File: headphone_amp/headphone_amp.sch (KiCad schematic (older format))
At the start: 41 parts, among them J1 Molex_SL_01x02_Male, J2 Molex_SL_01x02_Male, J3 Molex_SL_01x03_Male, J4 Molex_SL_01x03_Male, Q1 PZTA42, Q2 PZTA92, Q3 PZTA42, Q4 PZTA92, U1 NE5532

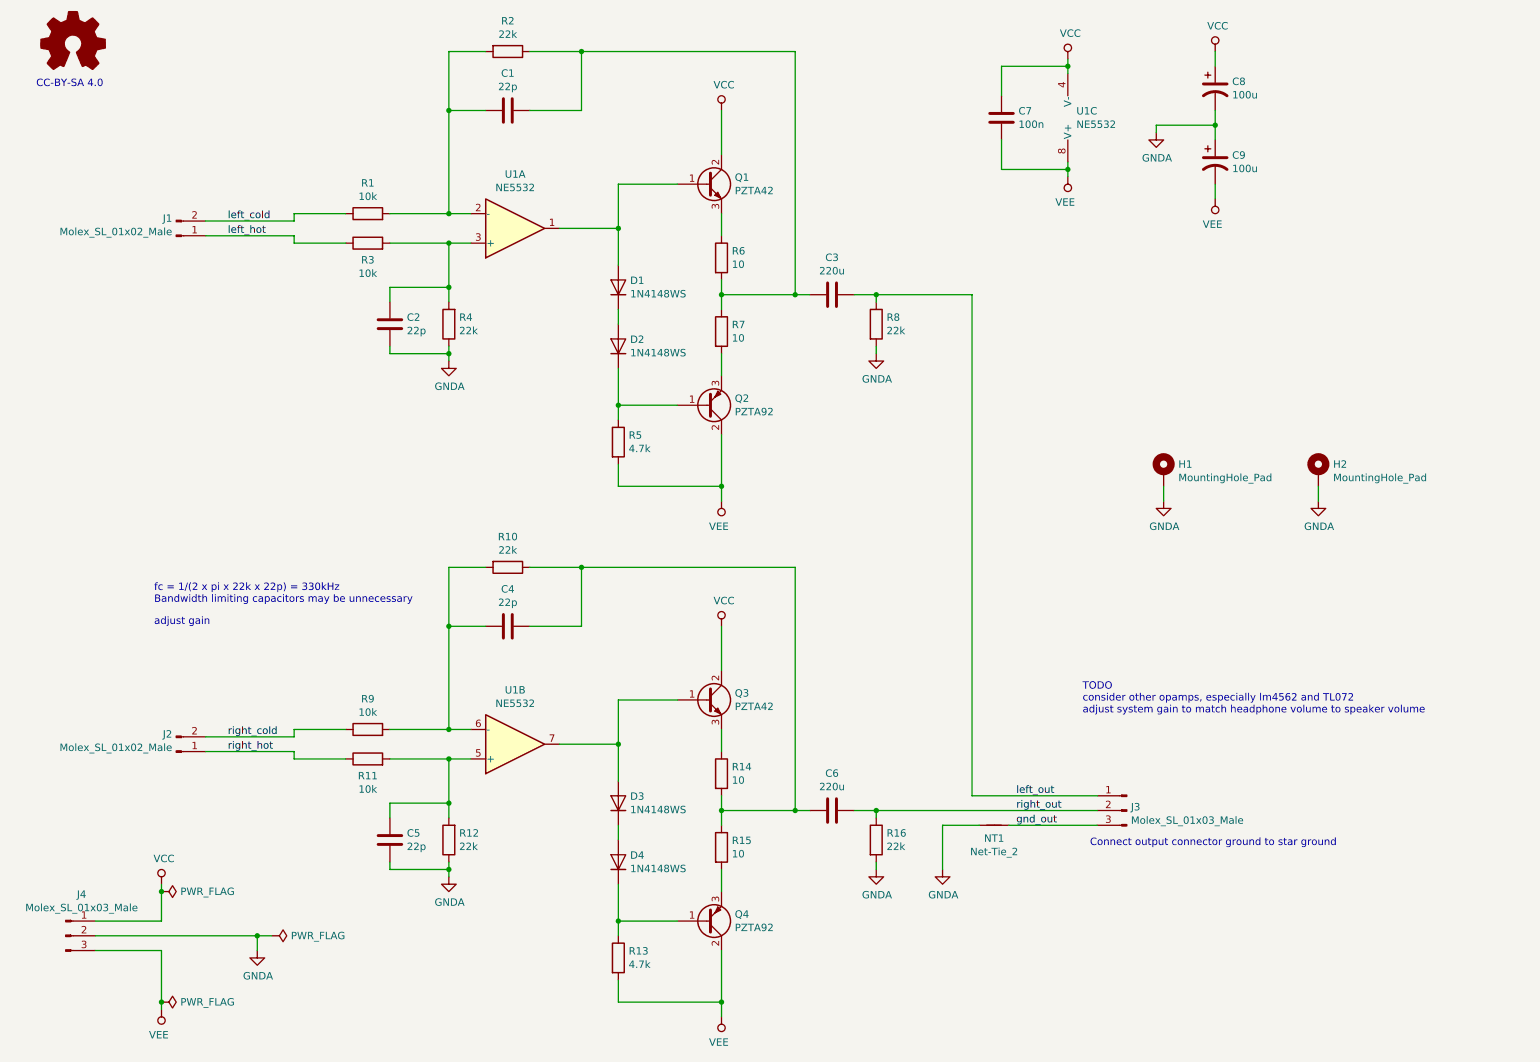
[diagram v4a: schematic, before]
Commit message: Update Headphone Amp to fix opamp power supplies
* fix opamp power supply connections. VCC was connected to V-, VEE to
V+. Fixed.
* re-layout opamp section to reflect above fix.
* right and left input connectors swapped to allow above fix.
* update schematic/layout date & revision in title block, and in board
silk.
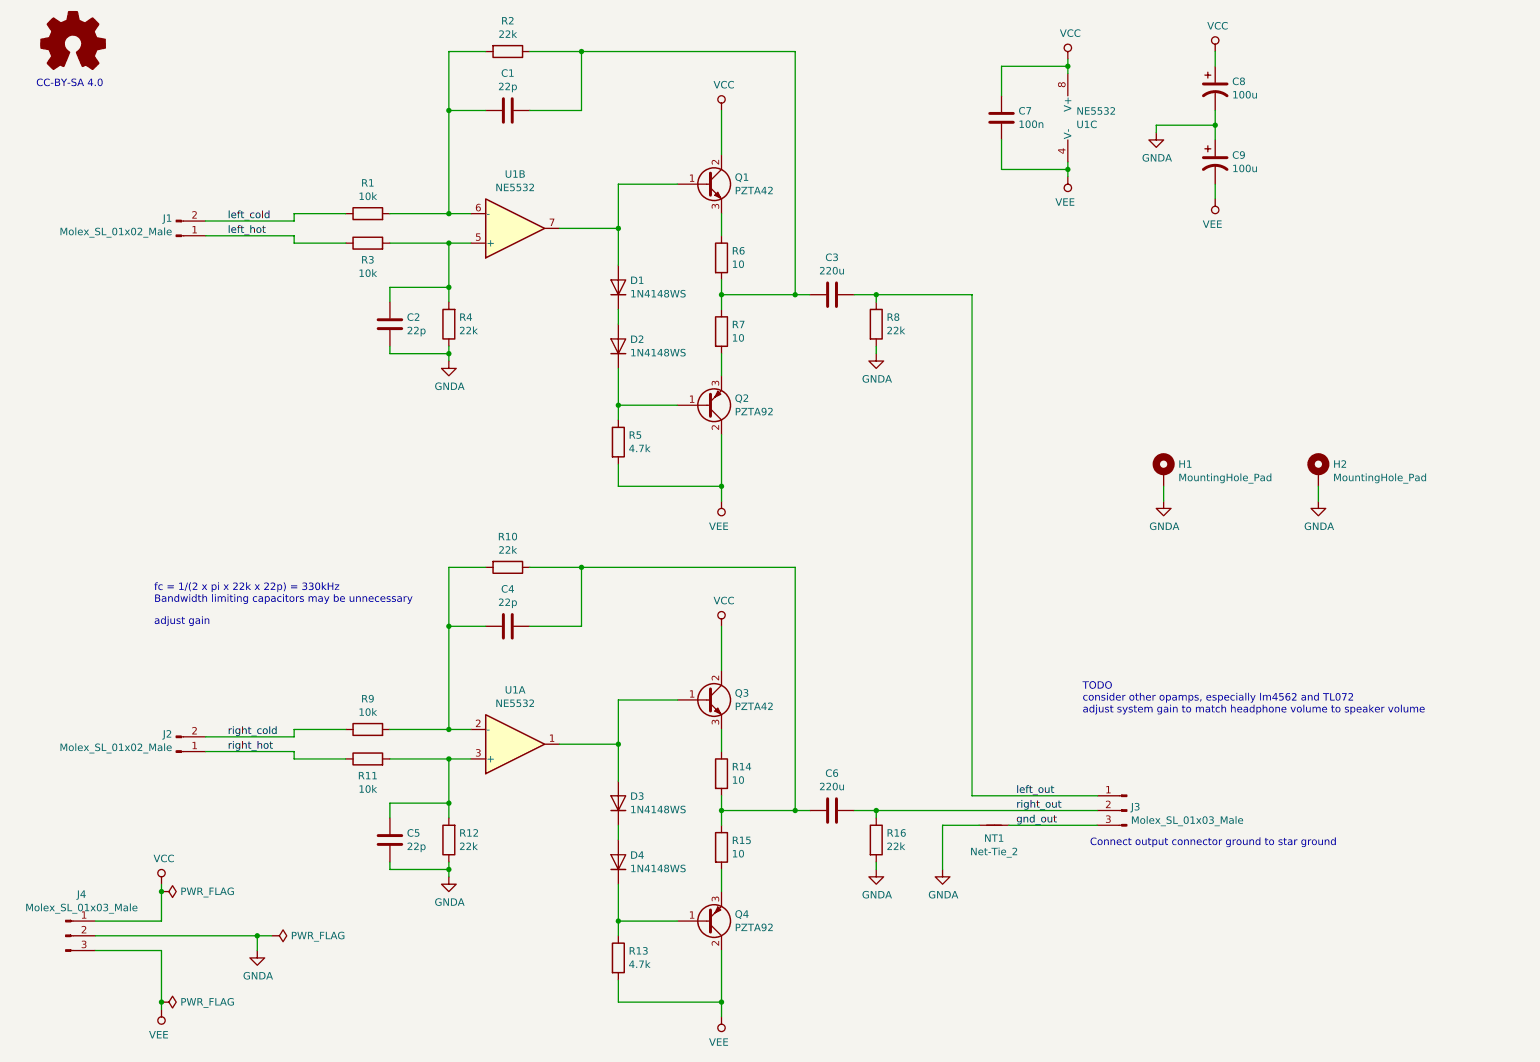
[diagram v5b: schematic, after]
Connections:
- net VCC: now also U1.8 (V+); no longer U1.4 (V-)
- net VEE: now also U1.4 (V-); no longer U1.8 (V+)
- net at D1.2 (A), Q1.1 (B): now also U1.7; no longer U1.1
- net at C1.2, R1.2, R2.2: now also U1.6 (-); no longer U1.2 (-)
- net at C2.1, R3.2, R4.2: now also U1.5 (+); no longer U1.3 (+)
- net at D3.2 (A), Q3.1 (B): now also U1.1; no longer U1.7
- net at C4.2, R10.2, R9.2: now also U1.2 (-); no longer U1.6 (-)
- net at C5.1, R11.2, R12.2: now also U1.3 (+); no longer U1.5 (+)
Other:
- moved on the sheet: U1A, U1B
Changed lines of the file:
@@
 Sheet 1 1
 Title "Headphone Amplifier"
-Date "2019-09-14"
-Rev "0"
+Date "2019-10-13"
+Rev "1"
 Comp "G. Keeth"
 Comment1 "Preamp 2019"
@@
 Wire Wire Line
 	4350 900  5800 900
-$Comp
-L Amplifier_Operational:NE5532 U1
-U 1 1 5D8981A1
-P 3900 2100
-F 0 "U1" H 3900 1733 50  0000 C CNN
-F 1 "NE5532" H 3900 1824 50  0000 C CNN
-F 2 "Package_SO:SOIC-8_3.9x4.9mm_P1.27mm" H 3900 2100 50  0001 C CNN
-F 3 "http://www.ti.com/lit/ds/symlink/ne5532.pdf" H 3900 2100 50  0001 C CNN
-F 4 "ON Semiconductor" H 3900 2100 50  0001 C CNN "Manufacturer"
-F 5 "NE5532AD8R2G" H 3900 2100 50  0001 C CNN "Manufacturer PN"
-F 6 "Digikey" H 3900 2100 50  0001 C CNN "Distributor"
-F 7 "NE5532AD8R2GOSCT-ND" H 3900 2100 50  0001 C CNN "Distributor PN"
-F 8 "https://www.digikey.com/products/en?keywords=NE5532AD8R2GOSCT-ND" H 3900 2100 50  0001 C CNN "URL"
-F 9 "0.90" H 3900 2100 50  0001 C CNN "Unit Price"
-	1    3900 2100
-	1    0    0    1
-$EndComp
 Text Notes 1450 4650 0    50   ~ 0
 fc = 1/(2 x pi x 22k x 22p) = 330kHz\nBandwidth limiting capacitors may be unnecessary
@@
 Text Notes 7800 6300 0    50   ~ 0
 Connect output connector ground to star ground
-$Comp
-L Amplifier_Operational:NE5532 U1
-U 2 1 5D95A57F
-P 3900 5600
-F 0 "U1" H 3900 5233 50  0000 C CNN
-F 1 "NE5532" H 3900 5324 50  0000 C CNN
-F 2 "Package_SO:SOIC-8_3.9x4.9mm_P1.27mm" H 3900 5600 50  0001 C CNN
-F 3 "http://www.ti.com/lit/ds/symlink/ne5532.pdf" H 3900 5600 50  0001 C CNN
-F 4 "ON Semiconductor" H 3900 5600 50  0001 C CNN "Manufacturer"
-F 5 "NE5532AD8R2G" H 3900 5600 50  0001 C CNN "Manufacturer PN"
-F 6 "Digikey" H 3900 5600 50  0001 C CNN "Distributor"
-F 7 "NE5532AD8R2GOSCT-ND" H 3900 5600 50  0001 C CNN "Distributor PN"
-F 8 "https://www.digikey.com/products/en?keywords=NE5532AD8R2GOSCT-ND" H 3900 5600 50  0001 C CNN "URL"
-F 9 "0.90" H 3900 5600 50  0001 C CNN "Unit Price"
-	2    3900 5600
-	1    0    0    1
-$EndComp
-$Comp
-L Amplifier_Operational:NE5532 U1
-U 3 1 5D95E720
-P 7750 1350
-F 0 "U1" H 7708 1304 50  0000 L CNN
-F 1 "NE5532" H 7708 1395 50  0000 L CNN
-F 2 "Package_SO:SOIC-8_3.9x4.9mm_P1.27mm" H 7750 1350 50  0001 C CNN
-F 3 "http://www.ti.com/lit/ds/symlink/ne5532.pdf" H 7750 1350 50  0001 C CNN
-F 4 "ON Semiconductor" H 7750 1350 50  0001 C CNN "Manufacturer"
-F 5 "NE5532AD8R2G" H 7750 1350 50  0001 C CNN "Manufacturer PN"
-F 6 "Digikey" H 7750 1350 50  0001 C CNN "Distributor"
-F 7 "NE5532AD8R2GOSCT-ND" H 7750 1350 50  0001 C CNN "Distributor PN"
-F 8 "https://www.digikey.com/products/en?keywords=NE5532AD8R2GOSCT-ND" H 7750 1350 50  0001 C CNN "URL"
-F 9 "0.90" H 7750 1350 50  0001 C CNN "Unit Price"
-	3    7750 1350
-	1    0    0    1
-$EndComp
 $Comp
 L Device:CP1 C9
@@
 Wire Wire Line
 	6800 6150 7050 6150
+$Comp
+L Amplifier_Operational:NE5532 U1
+U 1 1 5D8981A1
+P 3900 5600
+F 0 "U1" H 3900 5233 50  0000 C CNN
+F 1 "NE5532" H 3900 5324 50  0000 C CNN
+F 2 "Package_SO:SOIC-8_3.9x4.9mm_P1.27mm" H 3900 5600 50  0001 C CNN
+F 3 "http://www.ti.com/lit/ds/symlink/ne5532.pdf" H 3900 5600 50  0001 C CNN
+F 4 "ON Semiconductor" H 3900 5600 50  0001 C CNN "Manufacturer"
+F 5 "NE5532AD8R2G" H 3900 5600 50  0001 C CNN "Manufacturer PN"
+F 6 "Digikey" H 3900 5600 50  0001 C CNN "Distributor"
+F 7 "NE5532AD8R2GOSCT-ND" H 3900 5600 50  0001 C CNN "Distributor PN"
+F 8 "https://www.digikey.com/products/en?keywords=NE5532AD8R2GOSCT-ND" H 3900 5600 50  0001 C CNN "URL"
+F 9 "0.90" H 3900 5600 50  0001 C CNN "Unit Price"
+	1    3900 5600
+	1    0    0    1
+$EndComp
+$Comp
+L Amplifier_Operational:NE5532 U1
+U 3 1 5D95E720
+P 7750 1350
+F 0 "U1" H 7708 1304 50  0000 L CNN
+F 1 "NE5532" H 7708 1395 50  0000 L CNN
+F 2 "Package_SO:SOIC-8_3.9x4.9mm_P1.27mm" H 7750 1350 50  0001 C CNN
+F 3 "http://www.ti.com/lit/ds/symlink/ne5532.pdf" H 7750 1350 50  0001 C CNN
+F 4 "ON Semiconductor" H 7750 1350 50  0001 C CNN "Manufacturer"
+F 5 "NE5532AD8R2G" H 7750 1350 50  0001 C CNN "Manufacturer PN"
+F 6 "Digikey" H 7750 1350 50  0001 C CNN "Distributor"
+F 7 "NE5532AD8R2GOSCT-ND" H 7750 1350 50  0001 C CNN "Distributor PN"
+F 8 "https://www.digikey.com/products/en?keywords=NE5532AD8R2GOSCT-ND" H 7750 1350 50  0001 C CNN "URL"
+F 9 "0.90" H 7750 1350 50  0001 C CNN "Unit Price"
+	3    7750 1350
+	1    0    0    -1
+$EndComp
+$Comp
+L Amplifier_Operational:NE5532 U1
+U 2 1 5D95A57F
+P 3900 2100
+F 0 "U1" H 3900 1733 50  0000 C CNN
+F 1 "NE5532" H 3900 1824 50  0000 C CNN
+F 2 "Package_SO:SOIC-8_3.9x4.9mm_P1.27mm" H 3900 2100 50  0001 C CNN
+F 3 "http://www.ti.com/lit/ds/symlink/ne5532.pdf" H 3900 2100 50  0001 C CNN
+F 4 "ON Semiconductor" H 3900 2100 50  0001 C CNN "Manufacturer"
+F 5 "NE5532AD8R2G" H 3900 2100 50  0001 C CNN "Manufacturer PN"
+F 6 "Digikey" H 3900 2100 50  0001 C CNN "Distributor"
+F 7 "NE5532AD8R2GOSCT-ND" H 3900 2100 50  0001 C CNN "Distributor PN"
+F 8 "https://www.digikey.com/products/en?keywords=NE5532AD8R2GOSCT-ND" H 3900 2100 50  0001 C CNN "URL"
+F 9 "0.90" H 3900 2100 50  0001 C CNN "Unit Price"
+	2    3900 2100
+	1    0    0    1
+$EndComp
 $EndSCHEMATC
